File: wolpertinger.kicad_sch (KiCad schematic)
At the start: 57 parts, among them IC1 TL074, IC2 TL074, K2 FRT5, K3 FRT5, Q1 BC549, T1 IN LEFT, T16 LED+, T17 LED-, T2 IN LEFT, T3 IN RIGHT, T4 IN RIGHT, T8 SWT, T9 SWT, U1 VTL5C, U2 VTL5C, U3 4093, U4 VTL5C, U5 VTL5C

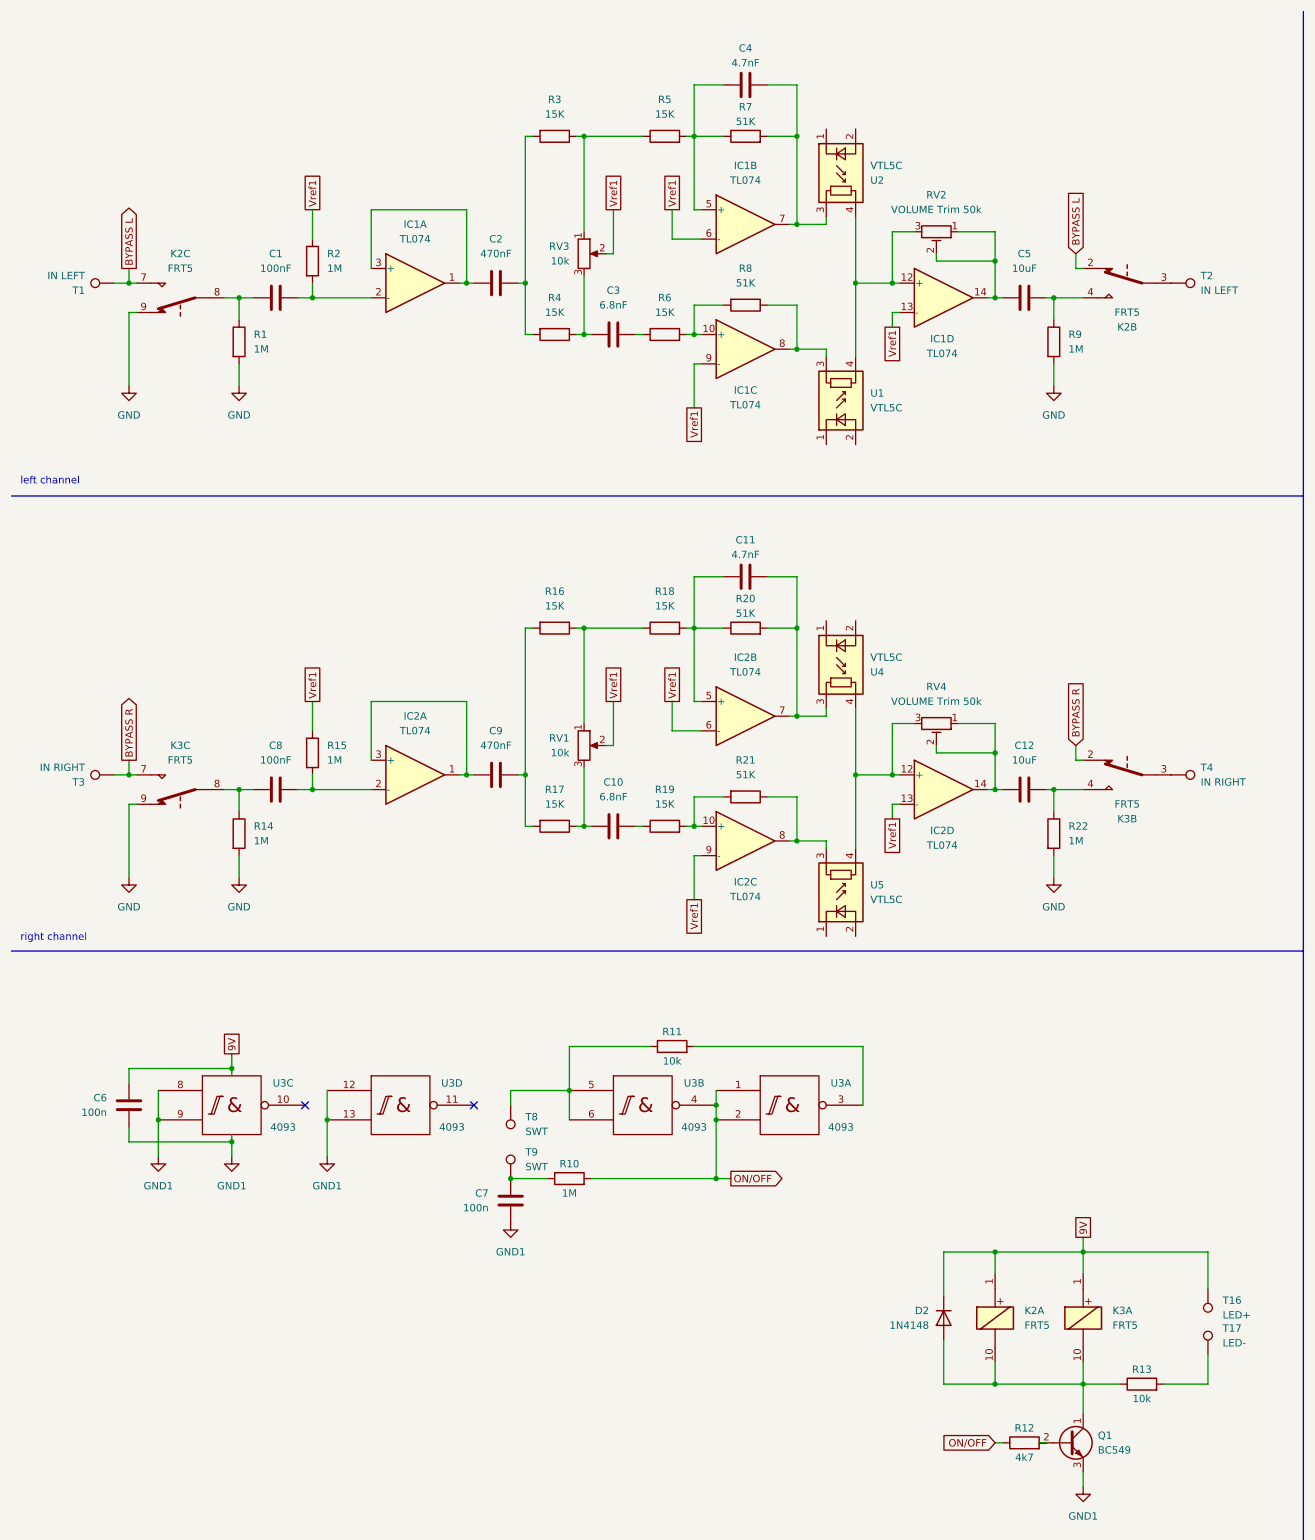
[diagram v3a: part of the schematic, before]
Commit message: Added PCB, Footprint cleanup
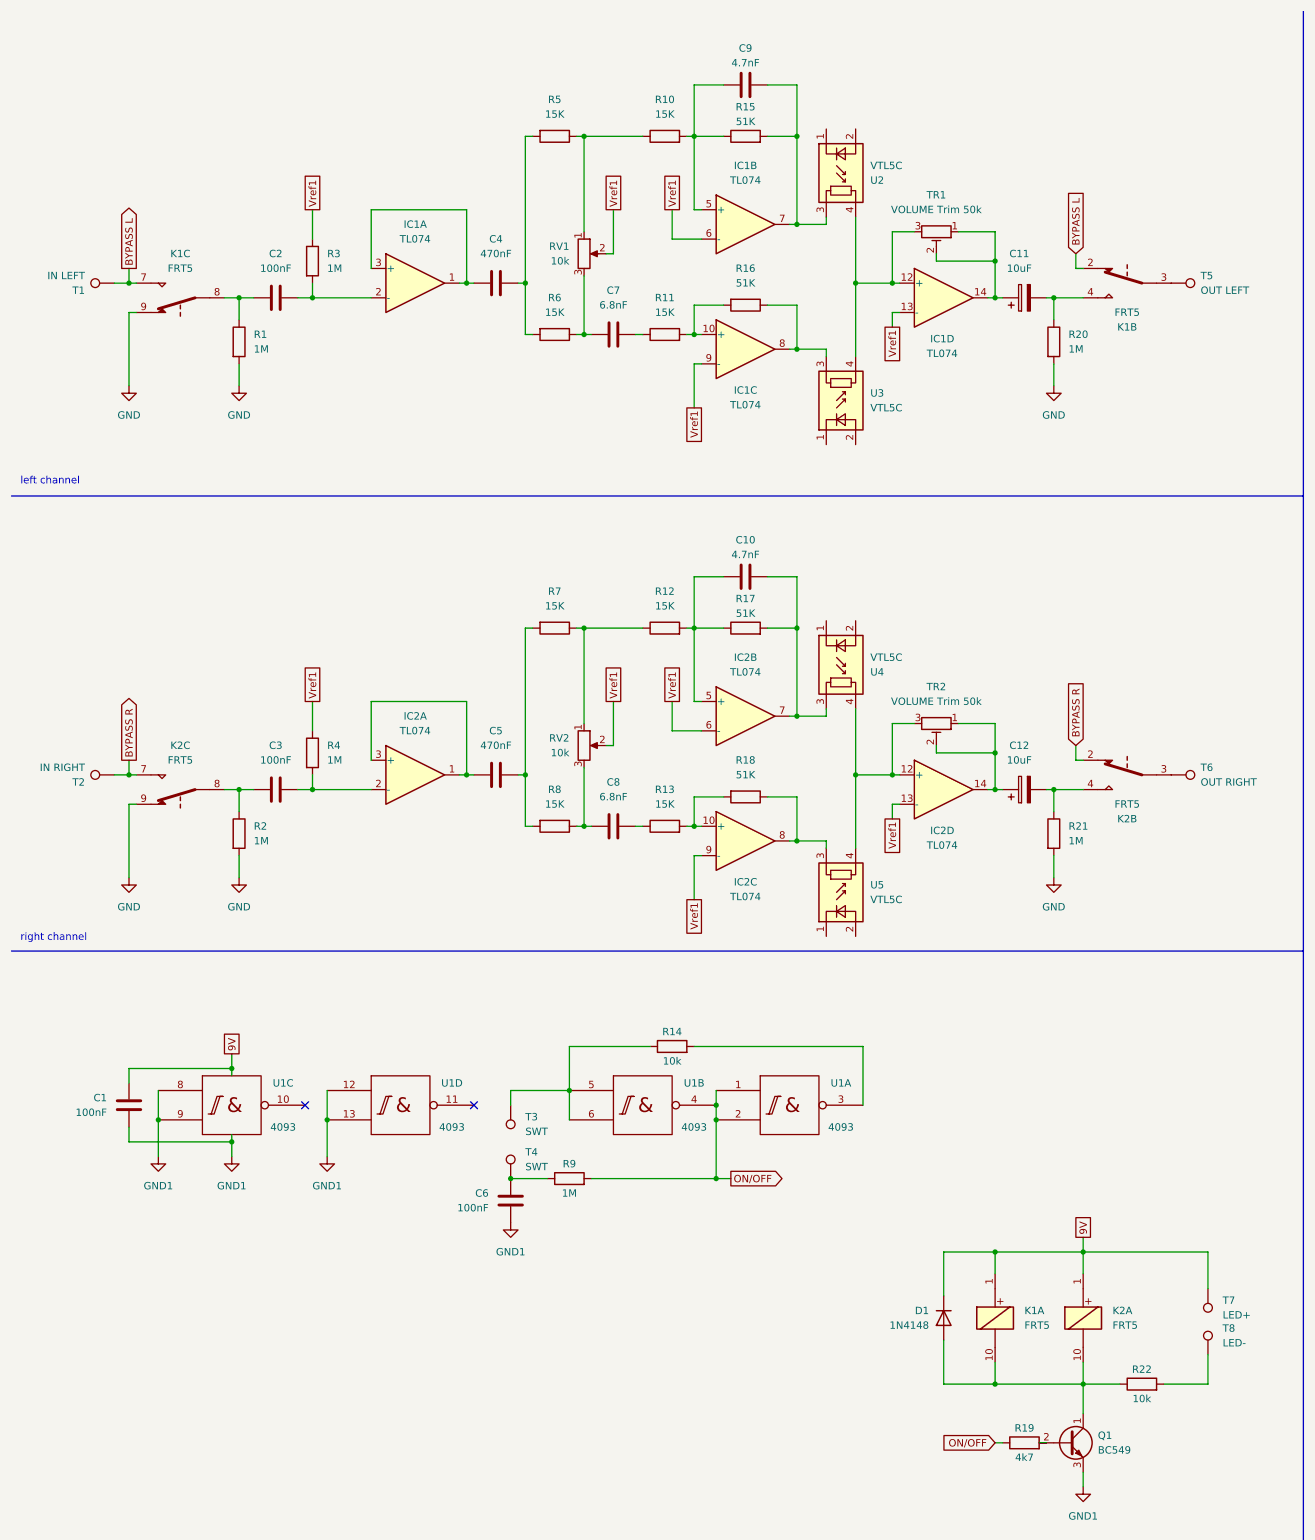
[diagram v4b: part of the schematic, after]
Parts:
- removed C12, C5: 10uF, symbol Device:C
- added C11, C12: 10uF, symbol Device:C_Polarized
- C1: renamed from C6; value 100n -> 100nF; footprint Capacitor_SMD:C_0805_2012Metric_Pad1.18x1.45mm_HandSolder -> (none)
- C6: renamed from C7; value 100n -> 100nF; footprint Capacitor_SMD:C_0805_2012Metric_Pad1.18x1.45mm_HandSolder -> (none)
- IC1, IC2: footprint (none) -> Package_DIP:CERDIP-14_W7.62mm_SideBrazed_LongPads_Socket
- R1: footprint (none) -> Resistor_THT:R_Axial_DIN0207_L6.3mm_D2.5mm_P7.62mm_Horizontal
- R10: renamed from R5; footprint (none) -> Resistor_THT:R_Axial_DIN0207_L6.3mm_D2.5mm_P7.62mm_Horizontal
- R11: renamed from R6; footprint (none) -> Resistor_THT:R_Axial_DIN0207_L6.3mm_D2.5mm_P7.62mm_Horizontal
- R12: renamed from R18; footprint (none) -> Resistor_THT:R_Axial_DIN0207_L6.3mm_D2.5mm_P7.62mm_Horizontal
- R13: renamed from R19; footprint (none) -> Resistor_THT:R_Axial_DIN0207_L6.3mm_D2.5mm_P7.62mm_Horizontal
- R14: renamed from R11; footprint Resistor_SMD:R_0805_2012Metric_Pad1.20x1.40mm_HandSolder -> Resistor_THT:R_Axial_DIN0207_L6.3mm_D2.5mm_P7.62mm_Horizontal
- R15: renamed from R7; footprint (none) -> Resistor_THT:R_Axial_DIN0207_L6.3mm_D2.5mm_P7.62mm_Horizontal
- R16: renamed from R8; footprint (none) -> Resistor_THT:R_Axial_DIN0207_L6.3mm_D2.5mm_P7.62mm_Horizontal
- R17: renamed from R20; footprint (none) -> Resistor_THT:R_Axial_DIN0207_L6.3mm_D2.5mm_P7.62mm_Horizontal
- R18: renamed from R21; footprint (none) -> Resistor_THT:R_Axial_DIN0207_L6.3mm_D2.5mm_P7.62mm_Horizontal
- R19: renamed from R12; footprint Resistor_SMD:R_0805_2012Metric_Pad1.20x1.40mm_HandSolder -> Resistor_THT:R_Axial_DIN0207_L6.3mm_D2.5mm_P7.62mm_Horizontal
- R2: renamed from R14; footprint (none) -> Resistor_THT:R_Axial_DIN0207_L6.3mm_D2.5mm_P7.62mm_Horizontal
- R20: renamed from R9; footprint (none) -> Resistor_THT:R_Axial_DIN0207_L6.3mm_D2.5mm_P7.62mm_Horizontal
- R21: renamed from R22; footprint (none) -> Resistor_THT:R_Axial_DIN0207_L6.3mm_D2.5mm_P7.62mm_Horizontal
- R22: renamed from R13; footprint Resistor_SMD:R_0805_2012Metric_Pad1.20x1.40mm_HandSolder -> Resistor_THT:R_Axial_DIN0207_L6.3mm_D2.5mm_P7.62mm_Horizontal
- R3: renamed from R2; footprint (none) -> Resistor_THT:R_Axial_DIN0207_L6.3mm_D2.5mm_P7.62mm_Horizontal
- R4: renamed from R15; footprint (none) -> Resistor_THT:R_Axial_DIN0207_L6.3mm_D2.5mm_P7.62mm_Horizontal
- R5: renamed from R3; footprint (none) -> Resistor_THT:R_Axial_DIN0207_L6.3mm_D2.5mm_P7.62mm_Horizontal
- R6: renamed from R4; footprint (none) -> Resistor_THT:R_Axial_DIN0207_L6.3mm_D2.5mm_P7.62mm_Horizontal
- R7: renamed from R16; footprint (none) -> Resistor_THT:R_Axial_DIN0207_L6.3mm_D2.5mm_P7.62mm_Horizontal
- R8: renamed from R17; footprint (none) -> Resistor_THT:R_Axial_DIN0207_L6.3mm_D2.5mm_P7.62mm_Horizontal
- R9: renamed from R10; footprint Resistor_SMD:R_0805_2012Metric_Pad1.20x1.40mm_HandSolder -> Resistor_THT:R_Axial_DIN0207_L6.3mm_D2.5mm_P7.62mm_Horizontal
- T5: renamed from T2; value IN LEFT -> OUT LEFT
- T6: renamed from T4; value IN RIGHT -> OUT RIGHT
- U1: renamed from U3; footprint Package_SO:SO-14_3.9x8.65mm_P1.27mm -> Package_DIP:CERDIP-14_W7.62mm_SideBrazed_LongPads_Socket
- renumbered C11 to C10, C1 to C2, C8 to C3, C2 to C4, C9 to C5, C3 to C7, C10 to C8, C4 to C9, D2 to D1, K2 to K1, K3 to K2, RV3 to RV1, RV1 to RV2, T3 to T2, T8 to T3, T9 to T4, T16 to T7, T17 to T8, RV2 to TR1, RV4 to TR2, U1 to U3
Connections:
- net at K2.4, R21.1: now also C12.2
- net at IC2.14, TR2.1, TR2.2: now also C12.1
- net at IC1.14, TR1.1, TR1.2: now also C11.1
- net at K1.4, R20.1: now also C11.2

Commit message: Add footprints
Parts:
- C1, C2, C3, C6: footprint (none) -> Capacitor_THT:C_Rect_L7.2mm_W2.5mm_P5.00mm_FKS2_FKP2_MKS2_MKP2
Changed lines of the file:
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@@
 			)
 		)
-		(property "Footprint" ""
+		(property "Footprint" "Capacitor_THT:C_Rect_L7.2mm_W2.5mm_P5.00mm_FKS2_FKP2_MKS2_MKP2"
 			(at 100.0252 222.25 0)
 			(effects
@@
 			)
 		)
-		(property "Footprint" ""
+		(property "Footprint" "Capacitor_THT:C_Rect_L7.2mm_W2.5mm_P5.00mm_FKS2_FKP2_MKS2_MKP2"
 			(at 33.9852 205.74 0)
 			(effects
@@
 			)
 		)
-		(property "Footprint" ""
+		(property "Footprint" "Capacitor_THT:C_Rect_L7.2mm_W2.5mm_P5.00mm_FKS2_FKP2_MKS2_MKP2"
 			(at 62.23 146.3548 0)
 			(effects
@@
 			)
 		)
-		(property "Footprint" ""
+		(property "Footprint" "Capacitor_THT:C_Rect_L7.2mm_W2.5mm_P5.00mm_FKS2_FKP2_MKS2_MKP2"
 			(at 62.23 61.2648 0)
 			(effects
